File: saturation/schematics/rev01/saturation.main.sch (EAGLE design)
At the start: 37 parts, among them IC1 TL084P, J1 OUT, J2 IN

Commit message: Inital saturation board layout
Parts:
- C1: value 2.2nF -> 0.1uF
- C2: value 22nF -> 0.1uF
- C5: value 100uF -> 0.1uF; device _common:CE-USE5-8.5 -> _common:CC-US025-024X044
- C6: value 0.1uF -> 2.2nF
- C7: value 0.1uF -> 22nF
- C8: value 0.1uF -> 100uF; device _common:CC-US025-024X044 -> _common:CE-USE5-8.5
- J1: value OUT -> IN
- J2: value IN -> OUT
- R10, R9: value 200K -> 10K; device pot:3RP/1610N -> _common:R
- R11: value 200K -> 22K; device pot:3RP/1610N -> _common:R
- R13: value 1M -> (none)
- R14: value 10K -> 200K; device _common:R -> pot:3RP/1610N
- R3: value 22K -> (none)
- R4: value 2.2K -> 1M
- R5: value 1M -> 200K; device _common:R -> pot:3RP/1610N
- R6: value 10K -> 1M
- R7: value (none) -> 2.2K
- R8: value (none) -> 200K; device _common:R -> pot:3RP/1610N
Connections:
- net +12V: now also C1.1, C5.1; no longer C6.1, C7.1
- net -12V: now also C2.2, C4.-, C5.2; no longer C5.-, C6.2, C8.2
- net 0V: now also C1.2, C2.1, C4.+, R2.1, R5.E, R7.1; no longer C5.+, C7.2, C8.1, R10.E, R5.1, R8.1
- net N$1: now also R10.1, R9.2; no longer R1.2, R2.1
- net N$10: now also R13.2, R14.A; no longer R8.2, R9.A
- net N$11: now also C8.+, R14.E, R14.S; no longer C4.+, R9.E, R9.S
- net N$12: now also C8.-, J2.HOT; no longer C4.-, J1.HOT
- net N$14: now also R8.E, R8.S, R9.1; no longer R1.1, R11.E, R11.S
- net N$15: now also C6.1, R7.2; no longer C1.1, R4.2
- net N$16: now also J1.HOT, R1.1; no longer J2.HOT, R14.1
- net N$17: now also R1.2, R2.2; no longer R14.2, R6.2
- net N$18: now also R3.1; no longer R7.1
- net N$19: now also R3.2, R4.2, R5.A; no longer R10.A, R13.2, R7.2
- net N$2: now also C7.2; no longer C2.2
- net N$20: now also C6.2, R8.A; no longer C1.2, R11.A
- net N$21: now also R5.S, R6.2; no longer R10.S, R5.2
- net N$4: now also D5.A, D6.C, S1.2; no longer D5.C, D6.A, S2.2
- net N$5: now also R10.2; no longer R2.2
- net N$6: now also D5.C, D6.A, S2.2; no longer D5.A, D6.C, S3.2
- net N$7: now also R11.1; no longer R3.1
- net N$8: now also S3.2; no longer S1.2
- net N$9: now also C7.1, R11.2; no longer C2.1, R3.2
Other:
- moved on the sheet: C1, C2, C4, C5, C6, C7, C8, D5, D6, J1, J2, R1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

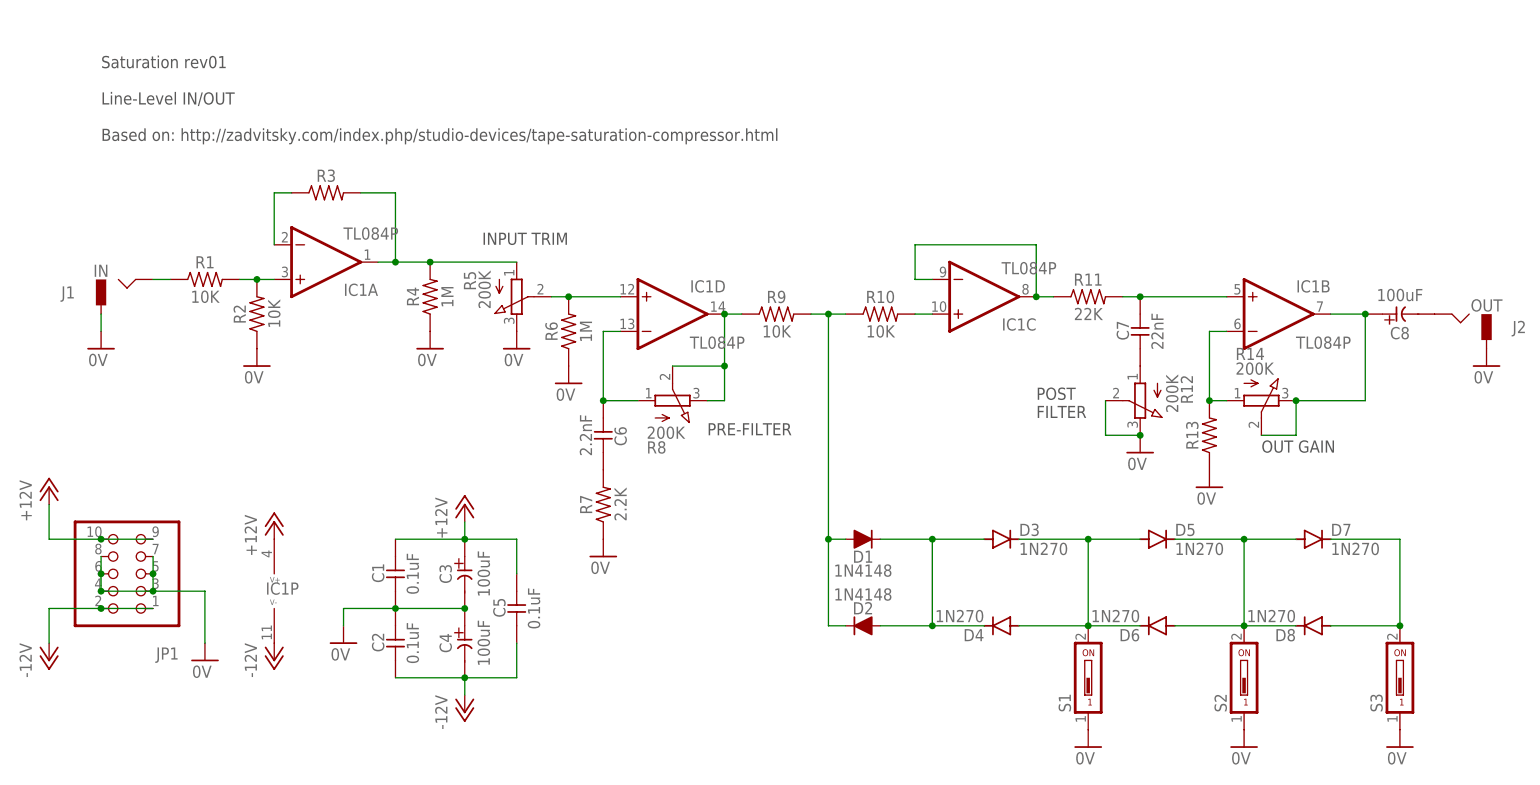
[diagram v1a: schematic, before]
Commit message: Routing for saturation
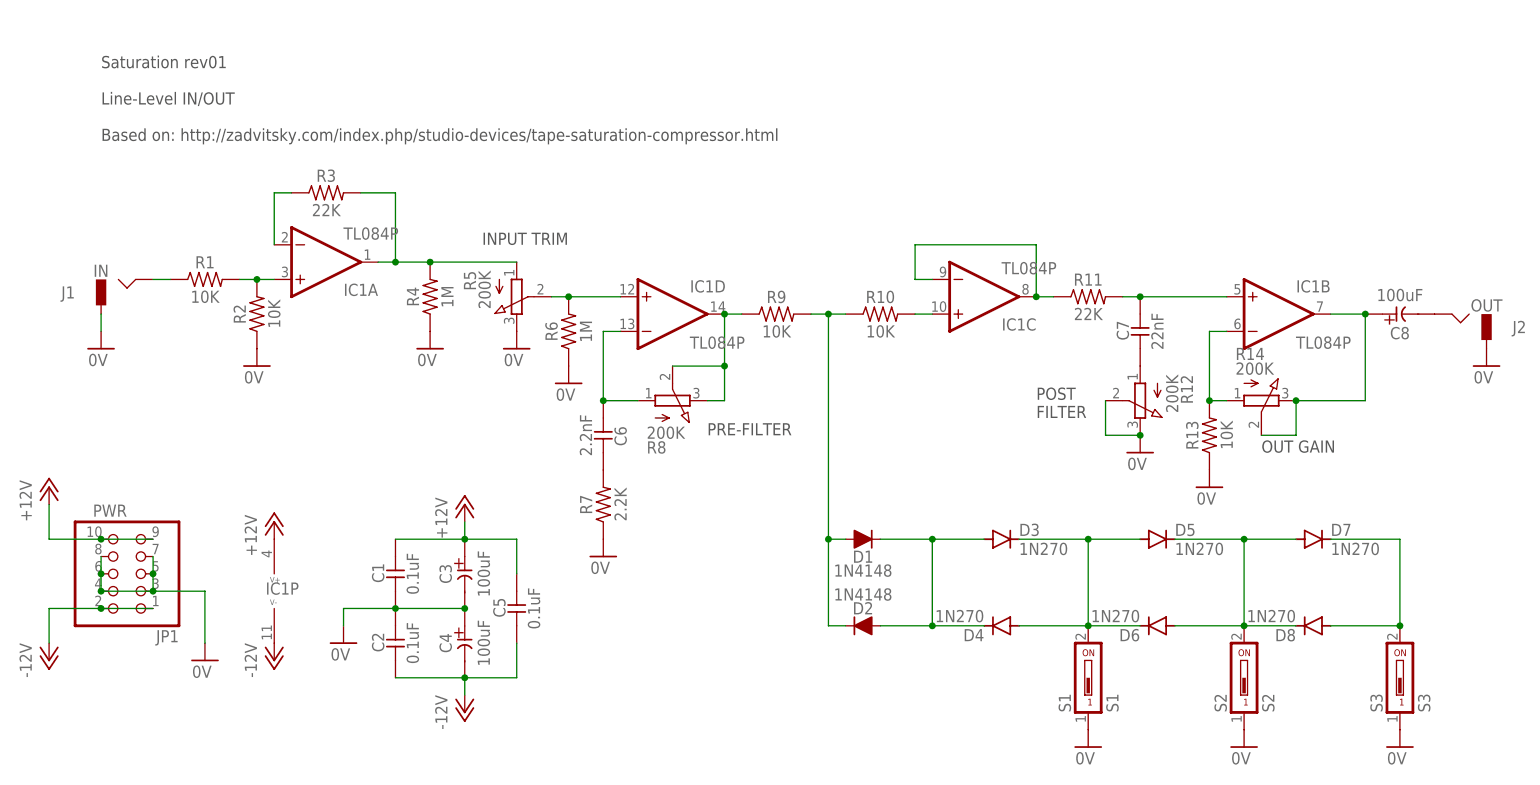
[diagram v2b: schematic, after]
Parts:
- JP1: value (none) -> PWR
- R13: value (none) -> 10K
- R3: value (none) -> 22K
- S1: value (none) -> S1
- S2: value (none) -> S2
- S3: value (none) -> S3
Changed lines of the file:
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@@
 </variantdefs>
 <classes>
-<class number="0" name="default" width="0" drill="0">
+<class number="0" name="default" width="0.4064" drill="0">
+</class>
+<class number="1" name="power" width="0.8128" drill="0">
 </class>
 </classes>
@@
 <part name="GND9" library="supply1" library_urn="urn:adsk.eagle:library:371" deviceset="0V" device=""/>
 <part name="GND12" library="supply1" library_urn="urn:adsk.eagle:library:371" deviceset="0V" device=""/>
-<part name="S3" library="switch-dil" library_urn="urn:adsk.eagle:library:375" deviceset="DS01" device="" package3d_urn="urn:adsk.eagle:package:27201/2"/>
-<part name="S1" library="switch-dil" library_urn="urn:adsk.eagle:library:375" deviceset="DS01" device="" package3d_urn="urn:adsk.eagle:package:27201/2"/>
-<part name="S2" library="switch-dil" library_urn="urn:adsk.eagle:library:375" deviceset="DS01" device="" package3d_urn="urn:adsk.eagle:package:27201/2"/>
+<part name="S3" library="switch-dil" library_urn="urn:adsk.eagle:library:375" deviceset="DS01" device="" package3d_urn="urn:adsk.eagle:package:27201/2" value="S3"/>
+<part name="S1" library="switch-dil" library_urn="urn:adsk.eagle:library:375" deviceset="DS01" device="" package3d_urn="urn:adsk.eagle:package:27201/2" value="S1"/>
+<part name="S2" library="switch-dil" library_urn="urn:adsk.eagle:library:375" deviceset="DS01" device="" package3d_urn="urn:adsk.eagle:package:27201/2" value="S2"/>
 <part name="R9" library="_common" deviceset="R" device="" value="10K"/>
 <part name="R10" library="_common" deviceset="R" device="" value="10K"/>
@@
 <part name="R6" library="_common" deviceset="R" device="" value="1M"/>
 <part name="R2" library="_common" deviceset="R" device="" value="10K"/>
-<part name="R3" library="_common" deviceset="R" device=""/>
+<part name="R3" library="_common" deviceset="R" device="" value="22K"/>
 <part name="C6" library="_common" deviceset="CC-US" device="025-024X044" value="2.2nF"/>
 <part name="C7" library="_common" deviceset="CC-US" device="025-024X044" value="22nF"/>
@@
 <part name="R8" library="pot" library_urn="urn:adsk.eagle:library:331" deviceset="3RP/1610N" device="" package3d_urn="urn:adsk.eagle:package:22726/1" value="200K"/>
 <part name="R12" library="pot" library_urn="urn:adsk.eagle:library:331" deviceset="3RP/1610N" device="" package3d_urn="urn:adsk.eagle:package:22726/1" value="200K"/>
-<part name="R13" library="_common" deviceset="R" device=""/>
+<part name="R13" library="_common" deviceset="R" device="" value="10K"/>
 <part name="GND11" library="supply1" library_urn="urn:adsk.eagle:library:371" deviceset="0V" device=""/>
 <part name="C8" library="_common" deviceset="CE-US" device="E5-8.5" value="100uF"/>
@@
 <part name="P+3" library="supply1" library_urn="urn:adsk.eagle:library:371" deviceset="+12V" device=""/>
 <part name="P-3" library="supply1" library_urn="urn:adsk.eagle:library:371" deviceset="-12V" device=""/>
-<part name="JP1" library="pinhead" library_urn="urn:adsk.eagle:library:325" deviceset="PINHD-2X5" device="" package3d_urn="urn:adsk.eagle:package:22470/2"/>
+<part name="JP1" library="pinhead" library_urn="urn:adsk.eagle:library:325" deviceset="PINHD-2X5" device="" package3d_urn="urn:adsk.eagle:package:22470/2" value="PWR"/>
 <part name="P-1" library="supply1" library_urn="urn:adsk.eagle:library:371" deviceset="-12V" device=""/>
 <part name="P+1" library="supply1" library_urn="urn:adsk.eagle:library:371" deviceset="+12V" device=""/>
@@
 </instance>
 <instance part="JP1" gate="A" x="-48.26" y="48.26" smashed="yes" rot="R180">
-<attribute name="NAME" x="-41.91" y="37.465" size="1.778" layer="95" rot="R180"/>
-<attribute name="VALUE" x="-41.91" y="63.5" size="1.778" layer="96" rot="R180"/>
+<attribute name="NAME" x="-41.91" y="40.005" size="1.778" layer="95" rot="R180"/>
+<attribute name="VALUE" x="-49.53" y="58.42" size="1.778" layer="96" rot="R180"/>
 </instance>
 <instance part="P-1" gate="1" x="-60.96" y="35.56" smashed="yes">
@@
 </segment>
 </net>
-<net name="0V" class="0">
+<net name="0V" class="1">
 <segment>
 <pinref part="GND13" gate="1" pin="0V"/>
@@
 </segment>
 </net>
-<net name="+12V" class="0">
+<net name="+12V" class="1">
 <segment>
 <pinref part="IC1" gate="P" pin="V+"/>
@@
 </segment>
 </net>
-<net name="-12V" class="0">
+<net name="-12V" class="1">
 <segment>
 <pinref part="IC1" gate="P" pin="V-"/>
@@
 </sheet>
 </sheets>
+<errors>
+</errors>
 </schematic>
 </drawing>

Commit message: Consolidate power on saturation board
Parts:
- R12, R14, R5, R8: device pot:3RP/1610N -> _common:3RP/1610N
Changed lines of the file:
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@@
 <part name="IC1" library="_common" deviceset="TL084" device="P"/>
 <part name="GND10" library="supply1" library_urn="urn:adsk.eagle:library:371" deviceset="0V" device=""/>
-<part name="R14" library="pot" library_urn="urn:adsk.eagle:library:331" deviceset="3RP/1610N" device="" package3d_urn="urn:adsk.eagle:package:22726/1" value="200K"/>
-<part name="R5" library="pot" library_urn="urn:adsk.eagle:library:331" deviceset="3RP/1610N" device="" package3d_urn="urn:adsk.eagle:package:22726/1" value="200K"/>
-<part name="R8" library="pot" library_urn="urn:adsk.eagle:library:331" deviceset="3RP/1610N" device="" package3d_urn="urn:adsk.eagle:package:22726/1" value="200K"/>
-<part name="R12" library="pot" library_urn="urn:adsk.eagle:library:331" deviceset="3RP/1610N" device="" package3d_urn="urn:adsk.eagle:package:22726/1" value="200K"/>
+<part name="R14" library="_common" deviceset="3RP/1610N" device="" package3d_urn="urn:adsk.eagle:package:22726/1" value="200K"/>
+<part name="R5" library="_common" deviceset="3RP/1610N" device="" package3d_urn="urn:adsk.eagle:package:22726/1" value="200K"/>
+<part name="R8" library="_common" deviceset="3RP/1610N" device="" package3d_urn="urn:adsk.eagle:package:22726/1" value="200K"/>
+<part name="R12" library="_common" deviceset="3RP/1610N" device="" package3d_urn="urn:adsk.eagle:package:22726/1" value="200K"/>
 <part name="R13" library="_common" deviceset="R" device="" value="10K"/>
 <part name="GND11" library="supply1" library_urn="urn:adsk.eagle:library:371" deviceset="0V" device=""/>
@@
 </segment>
 <segment>
-<pinref part="R13" gate="G$1" pin="1"/>
-<pinref part="GND11" gate="1" pin="0V"/>
-</segment>
-<segment>
-<pinref part="R7" gate="G$1" pin="1"/>
-<pinref part="GND8" gate="1" pin="0V"/>
-</segment>
-<segment>
 <pinref part="R6" gate="G$1" pin="1"/>
 <pinref part="GND7" gate="1" pin="0V"/>
@@
 <junction x="-45.72" y="48.26"/>
 </segment>
+<segment>
+<pinref part="R7" gate="G$1" pin="1"/>
+<pinref part="GND8" gate="1" pin="0V"/>
+</segment>
+<segment>
+<pinref part="R13" gate="G$1" pin="1"/>
+<pinref part="GND11" gate="1" pin="0V"/>
+</segment>
 </net>

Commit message: Saturation schem review
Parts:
- R2: value 10K -> 22K
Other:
- note added: "INPUT ATTEN"
- note added: "OUTUT GAIN"
- note added: "POST-FILTER AMOUNT"
- note added: "PRE-FILTER DRIVE"
- note removed: "INPUT TRIM"
- note removed: "OUT GAIN"
- note removed: "POST FILTER"
- note removed: "PRE-FILTER"
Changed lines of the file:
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@@
 <part name="R7" library="_common" deviceset="R" device="" value="2.2K"/>
 <part name="R6" library="_common" deviceset="R" device="" value="1M"/>
-<part name="R2" library="_common" deviceset="R" device="" value="10K"/>
+<part name="R2" library="_common" deviceset="R" device="" value="22K"/>
 <part name="R3" library="_common" deviceset="R" device="" value="22K"/>
 <part name="C6" library="_common" deviceset="CC-US" device="025-024X044" value="2.2nF"/>
@@
 Line-Level IN/OUT
 Based on: http://zadvitsky.com/index.php/studio-devices/tape-saturation-compressor.html</text>
-<text x="35.56" y="68.58" size="1.778" layer="97">PRE-FILTER</text>
-<text x="83.82" y="71.12" size="1.778" layer="97">POST
-FILTER</text>
-<text x="2.54" y="96.52" size="1.778" layer="97">INPUT TRIM</text>
-<text x="116.84" y="66.04" size="1.778" layer="97">OUT GAIN</text>
+<text x="35.56" y="66.04" size="1.778" layer="97">PRE-FILTER
+DRIVE</text>
+<text x="78.74" y="73.66" size="1.778" layer="97">POST-FILTER
+AMOUNT</text>
+<text x="5.08" y="96.52" size="1.778" layer="97">INPUT ATTEN</text>
+<text x="116.84" y="66.04" size="1.778" layer="97">OUTUT GAIN</text>
 </plain>
 <instances>

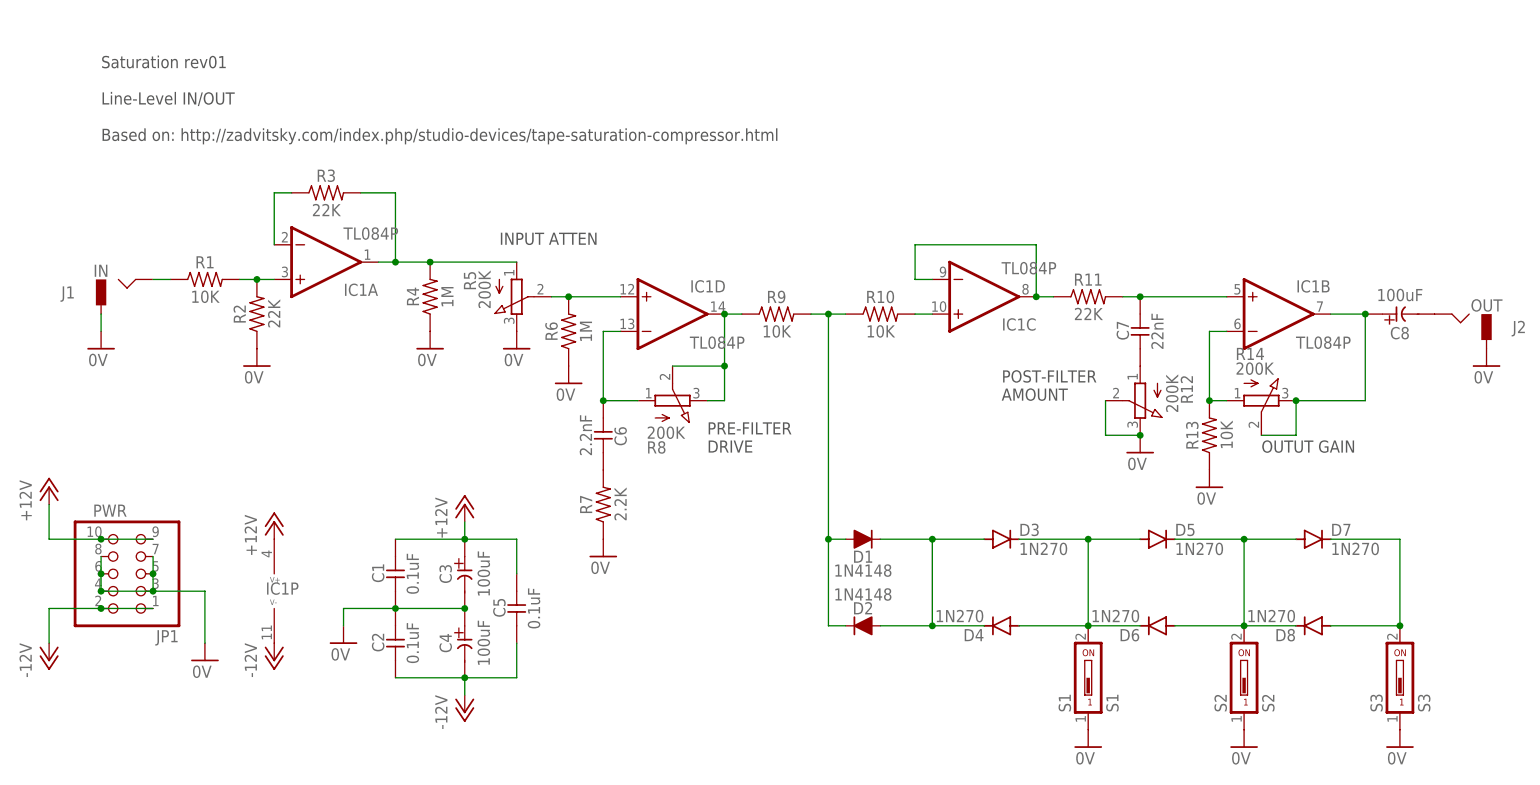
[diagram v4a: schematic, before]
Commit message: Update pot values
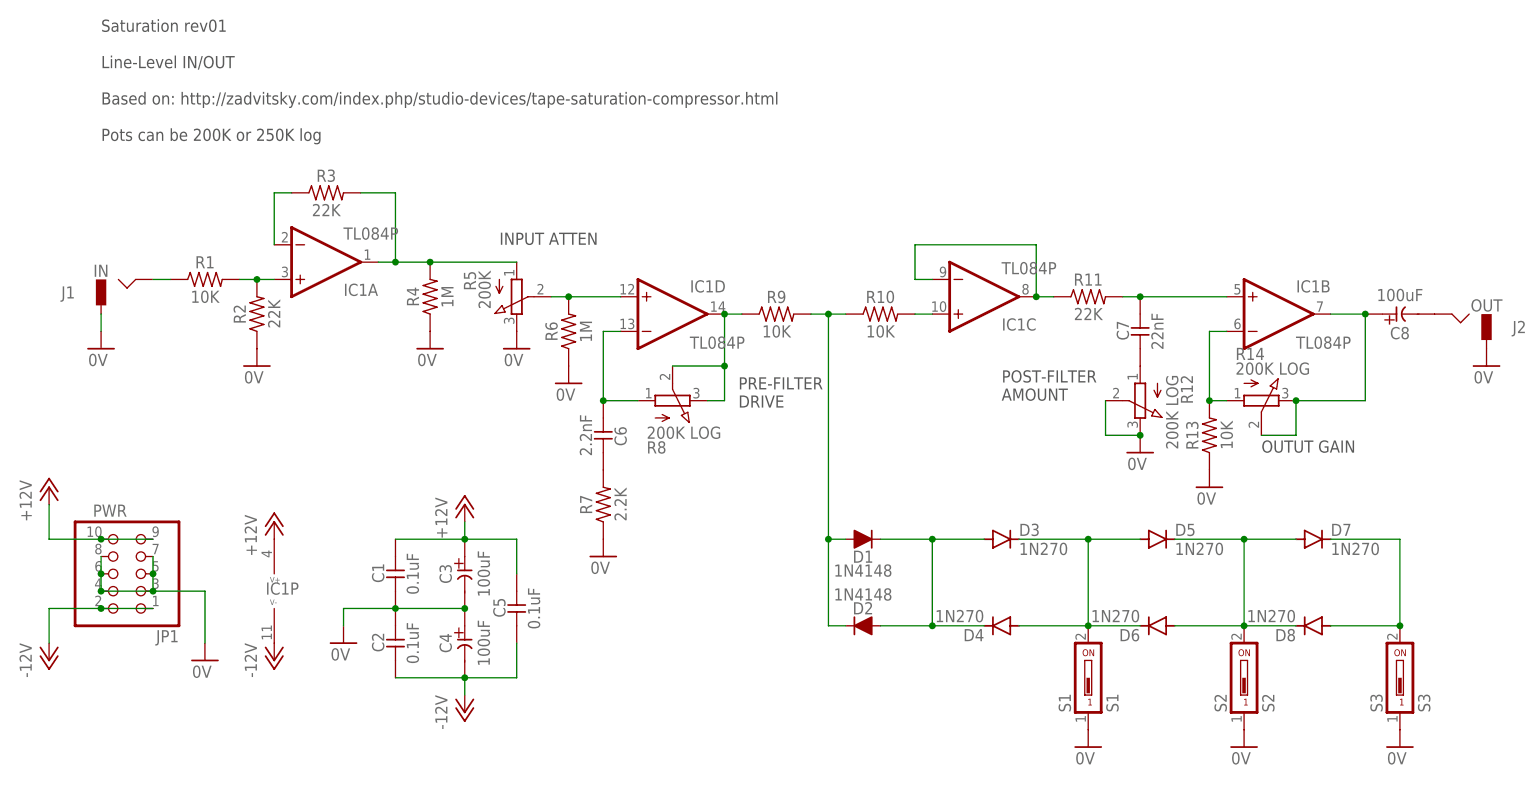
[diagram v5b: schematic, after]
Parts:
- R12, R14, R8: value 200K -> 200K LOG
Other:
- note added: "Saturation rev01 Line-Level IN/OUT Based on: http://zadvitsky.com/index.php/studio-devices/tape-saturation-compressor.html Pots can be 200K or 250K log"
- note removed: "Saturation rev01 Line-Level IN/OUT Based on: http://zadvitsky.com/index.php/studio-devices/tape-saturation-compressor.html"
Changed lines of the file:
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@@
 <?xml version="1.0" encoding="utf-8"?>
 <!DOCTYPE eagle SYSTEM "eagle.dtd">
-<eagle version="9.5.1">
+<eagle version="9.5.2">
 <drawing>
 <settings>
@@
 <part name="IC1" library="_common" deviceset="TL084" device="P"/>
 <part name="GND10" library="supply1" library_urn="urn:adsk.eagle:library:371" deviceset="0V" device=""/>
-<part name="R14" library="_common" deviceset="3RP/1610N" device="" package3d_urn="urn:adsk.eagle:package:22726/1" value="200K"/>
+<part name="R14" library="_common" deviceset="3RP/1610N" device="" package3d_urn="urn:adsk.eagle:package:22726/1" value="200K LOG"/>
 <part name="R5" library="_common" deviceset="3RP/1610N" device="" package3d_urn="urn:adsk.eagle:package:22726/1" value="200K"/>
-<part name="R8" library="_common" deviceset="3RP/1610N" device="" package3d_urn="urn:adsk.eagle:package:22726/1" value="200K"/>
-<part name="R12" library="_common" deviceset="3RP/1610N" device="" package3d_urn="urn:adsk.eagle:package:22726/1" value="200K"/>
+<part name="R8" library="_common" deviceset="3RP/1610N" device="" package3d_urn="urn:adsk.eagle:package:22726/1" value="200K LOG"/>
+<part name="R12" library="_common" deviceset="3RP/1610N" device="" package3d_urn="urn:adsk.eagle:package:22726/1" value="200K LOG"/>
 <part name="R13" library="_common" deviceset="R" device="" value="10K"/>
 <part name="GND11" library="supply1" library_urn="urn:adsk.eagle:library:371" deviceset="0V" device=""/>
@@
 <text x="-53.34" y="111.76" size="1.778" layer="97" font="vector">Saturation rev01
 Line-Level IN/OUT
-Based on: http://zadvitsky.com/index.php/studio-devices/tape-saturation-compressor.html</text>
-<text x="35.56" y="66.04" size="1.778" layer="97">PRE-FILTER
+Based on: http://zadvitsky.com/index.php/studio-devices/tape-saturation-compressor.html
+Pots can be 200K or 250K log</text>
+<text x="40.132" y="72.644" size="1.778" layer="97">PRE-FILTER
 DRIVE</text>
 <text x="78.74" y="73.66" size="1.778" layer="97">POST-FILTER
